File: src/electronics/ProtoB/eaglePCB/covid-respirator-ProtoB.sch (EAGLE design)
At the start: 59 parts, among them IC1 AD825R, IC2 L7805CV-DG, IC3 AD8607R, IC4 AD8607R, T2 BC548

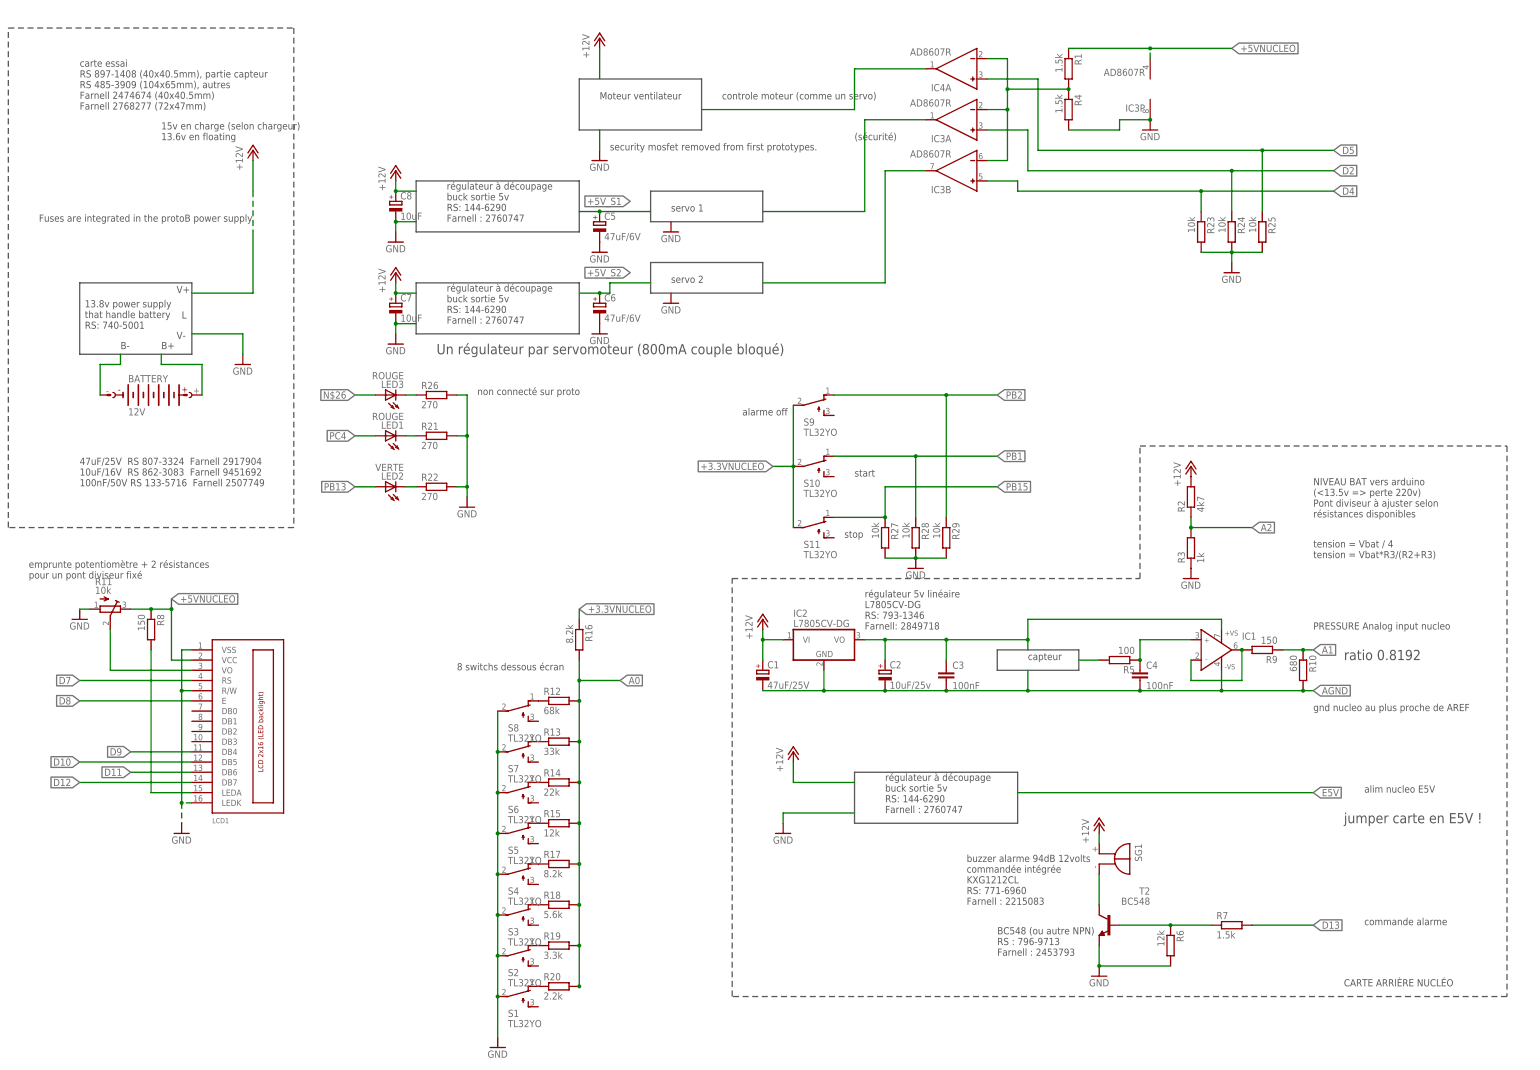
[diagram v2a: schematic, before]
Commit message: update protoB schematic
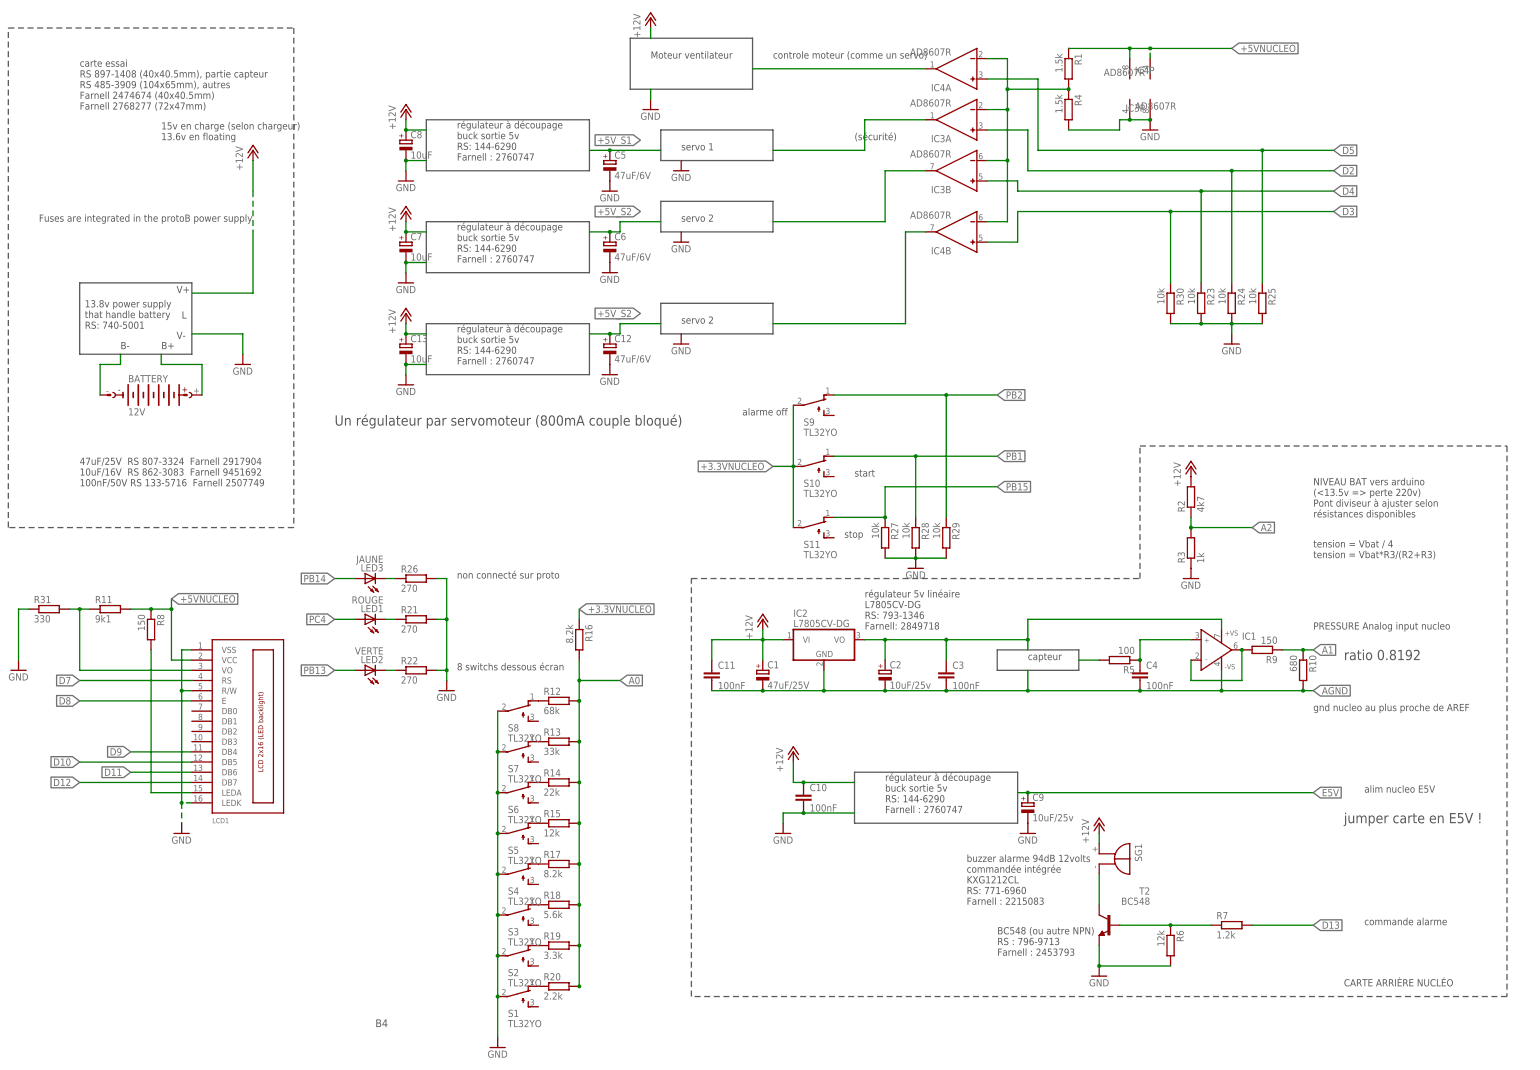
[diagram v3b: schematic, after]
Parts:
- added C10, C11: 100nF, rcl:C-EU050-050X075
- added C12: 47uF/6V, rcl:CPOL-EU150CLZ-1010
- added C13: 10uF, rcl:CPOL-EU150CLZ-1010
- added C9: 10uF/25v, rcl:CPOL-EU150CLZ-1010
- added R30: 10k, rcl:R-EU_0207/10
- added R31: 330, rcl:R-EU_0207/10
- LED3: value ROUGE -> JAUNE
- R11: value 10k -> 9k1; device pot:TRIM_EU-SM-42/43B -> rcl:R-EU_0207/10
- R7: value 1.5k -> 1.2k
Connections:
- net N$26 renamed PB14
- new net D3: IC4B.IN+, R30.1
- new net E5V: C9.+
- new net N$17: IC4B.OUT
- net +12V: now also C10.1, C11.1, C13.+
- net +5VNUCLEO: now also IC4P.V+, R11.2; no longer R11.E
- net +5V_S2: now also C12.+
- net AGND: now also C11.2
- net GND: now also C10.2, C12.-, C13.-, C9.-, IC4P.V-, R30.2, R31.1; no longer R11.A
- net N$10: now also R11.1, R31.2; no longer R11.S
- net N$4: now also IC4B.IN-
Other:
- note added: "B4"
- note removed: "emprunte potentiomètre + 2 résistances pour un pont diviseur fixé"
- note removed: "security mosfet removed from first prototypes."
- moved on the sheet: C5, C6, C7, C8, LED1, LED2, LED3, R21, R22, R23, R24, R25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

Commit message: schematic B5
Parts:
- added R32: 12k, rcl:R-EU_0207/10
- added R33: 100R, rcl:R-EU_0207/10
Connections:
- new net N$25: LCD1.DB7, R33.1
- new net PA13: LCD1.R/W, R32.2
- net D12: now also R33.2; no longer LCD1.DB7
- net GND: now also R32.1; no longer LCD1.R/W
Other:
- note added: "B5"
- note removed: "B4"
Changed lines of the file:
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@@
 <part name="R11" library="rcl" deviceset="R-EU_" device="0207/10" value="9k1"/>
 <part name="R31" library="rcl" deviceset="R-EU_" device="0207/10" value="330"/>
+<part name="R32" library="rcl" deviceset="R-EU_" device="0207/10" value="12k"/>
+<part name="R33" library="rcl" deviceset="R-EU_" device="0207/10" value="100R"/>
 </parts>
 <sheets>
@@
 <text x="152.4" y="15.24" size="1.778" layer="97">start</text>
 <text x="149.86" y="0" size="1.778" layer="97">stop</text>
-<text x="33.02" y="-121.92" size="1.9304" layer="97">B4</text>
+<text x="33.02" y="-121.92" size="1.9304" layer="97">B5</text>
 <wire x1="45.72" y1="53.34" x2="86.36" y2="53.34" width="0.1524" layer="97"/>
 <wire x1="86.36" y1="53.34" x2="86.36" y2="40.64" width="0.1524" layer="97"/>
@@
 <instance part="LCD1" gate="G$1" x="0" y="-27.94"/>
 <instance part="R8" gate="G$1" x="-22.86" y="-22.86" rot="R270"/>
-<instance part="GND11" gate="1" x="-15.24" y="-73.66"/>
+<instance part="GND11" gate="1" x="-15.24" y="-81.28"/>
 <instance part="GND12" gate="1" x="-55.88" y="-33.02"/>
 <instance part="S1" gate="BEF1" x="68.58" y="-114.3" rot="R270"/>
@@
 <instance part="R11" gate="G$1" x="-33.02" y="-17.78"/>
 <instance part="R31" gate="G$1" x="-48.26" y="-17.78"/>
+<instance part="R32" gate="G$1" x="-25.4" y="-71.12" rot="R90"/>
+<instance part="R33" gate="G$1" x="-40.64" y="-60.96" rot="R180"/>
 </instances>
 <busses>
@@
 <pinref part="GND11" gate="1" pin="GND"/>
 <wire x1="-12.7" y1="-66.04" x2="-15.24" y2="-66.04" width="0.1524" layer="91" style="longdash"/>
-<wire x1="-15.24" y1="-66.04" x2="-15.24" y2="-71.12" width="0.1524" layer="91" style="longdash"/>
-<wire x1="-15.24" y1="-66.04" x2="-15.24" y2="-38.1" width="0.1524" layer="91"/>
+<wire x1="-15.24" y1="-66.04" x2="-15.24" y2="-76.2" width="0.1524" layer="91" style="longdash"/>
+<wire x1="-15.24" y1="-76.2" x2="-15.24" y2="-78.74" width="0.1524" layer="91" style="longdash"/>
+<wire x1="-15.24" y1="-66.04" x2="-15.24" y2="-27.94" width="0.1524" layer="91"/>
 <junction x="-15.24" y="-66.04"/>
 <pinref part="LCD1" gate="G$1" pin="VSS"/>
-<wire x1="-15.24" y1="-38.1" x2="-15.24" y2="-27.94" width="0.1524" layer="91"/>
 <wire x1="-15.24" y1="-27.94" x2="-12.7" y2="-27.94" width="0.1524" layer="91"/>
-<pinref part="LCD1" gate="G$1" pin="R/W"/>
-<wire x1="-12.7" y1="-38.1" x2="-15.24" y2="-38.1" width="0.1524" layer="91"/>
-<junction x="-15.24" y="-38.1"/>
+<pinref part="R32" gate="G$1" pin="1"/>
+<wire x1="-25.4" y1="-76.2" x2="-15.24" y2="-76.2" width="0.1524" layer="91"/>
+<junction x="-15.24" y="-76.2"/>
 </segment>
 <segment>
@@
 <net name="D12" class="0">
 <segment>
-<pinref part="LCD1" gate="G$1" pin="DB7"/>
-<wire x1="-12.7" y1="-60.96" x2="-40.64" y2="-60.96" width="0.1524" layer="91"/>
-<label x="-40.64" y="-60.96" size="1.778" layer="95" rot="R180" xref="yes"/>
+<label x="-53.34" y="-60.96" size="1.778" layer="95" rot="R180" xref="yes"/>
+<pinref part="R33" gate="G$1" pin="2"/>
+<wire x1="-45.72" y1="-60.96" x2="-53.34" y2="-60.96" width="0.1524" layer="91"/>
 </segment>
 </net>
@@
 </segment>
 </net>
+<net name="PA13" class="0">
+<segment>
+<pinref part="LCD1" gate="G$1" pin="R/W"/>
+<wire x1="-12.7" y1="-38.1" x2="-25.4" y2="-38.1" width="0.1524" layer="91"/>
+<label x="-33.02" y="-38.1" size="1.778" layer="95" rot="R180" xref="yes"/>
+<pinref part="R32" gate="G$1" pin="2"/>
+<wire x1="-25.4" y1="-38.1" x2="-33.02" y2="-38.1" width="0.1524" layer="91"/>
+<wire x1="-25.4" y1="-66.04" x2="-25.4" y2="-38.1" width="0.1524" layer="91"/>
+<junction x="-25.4" y="-38.1"/>
+</segment>
+</net>
+<net name="N$25" class="0">
+<segment>
+<pinref part="R33" gate="G$1" pin="1"/>
+<pinref part="LCD1" gate="G$1" pin="DB7"/>
+<wire x1="-35.56" y1="-60.96" x2="-12.7" y2="-60.96" width="0.1524" layer="91"/>
+</segment>
+</net>

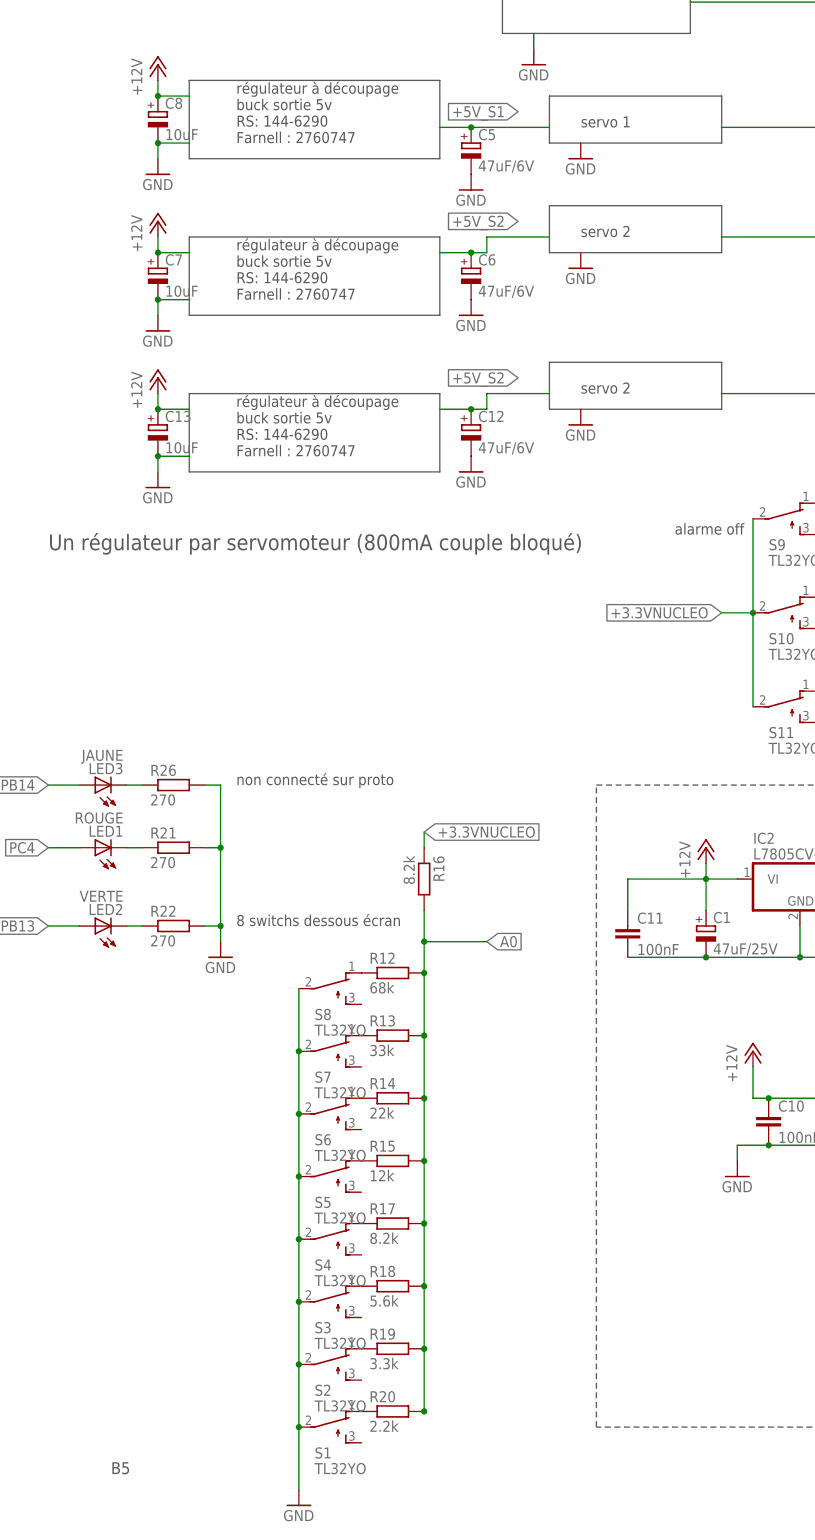
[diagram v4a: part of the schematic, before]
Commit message: schematic B6 with servo names
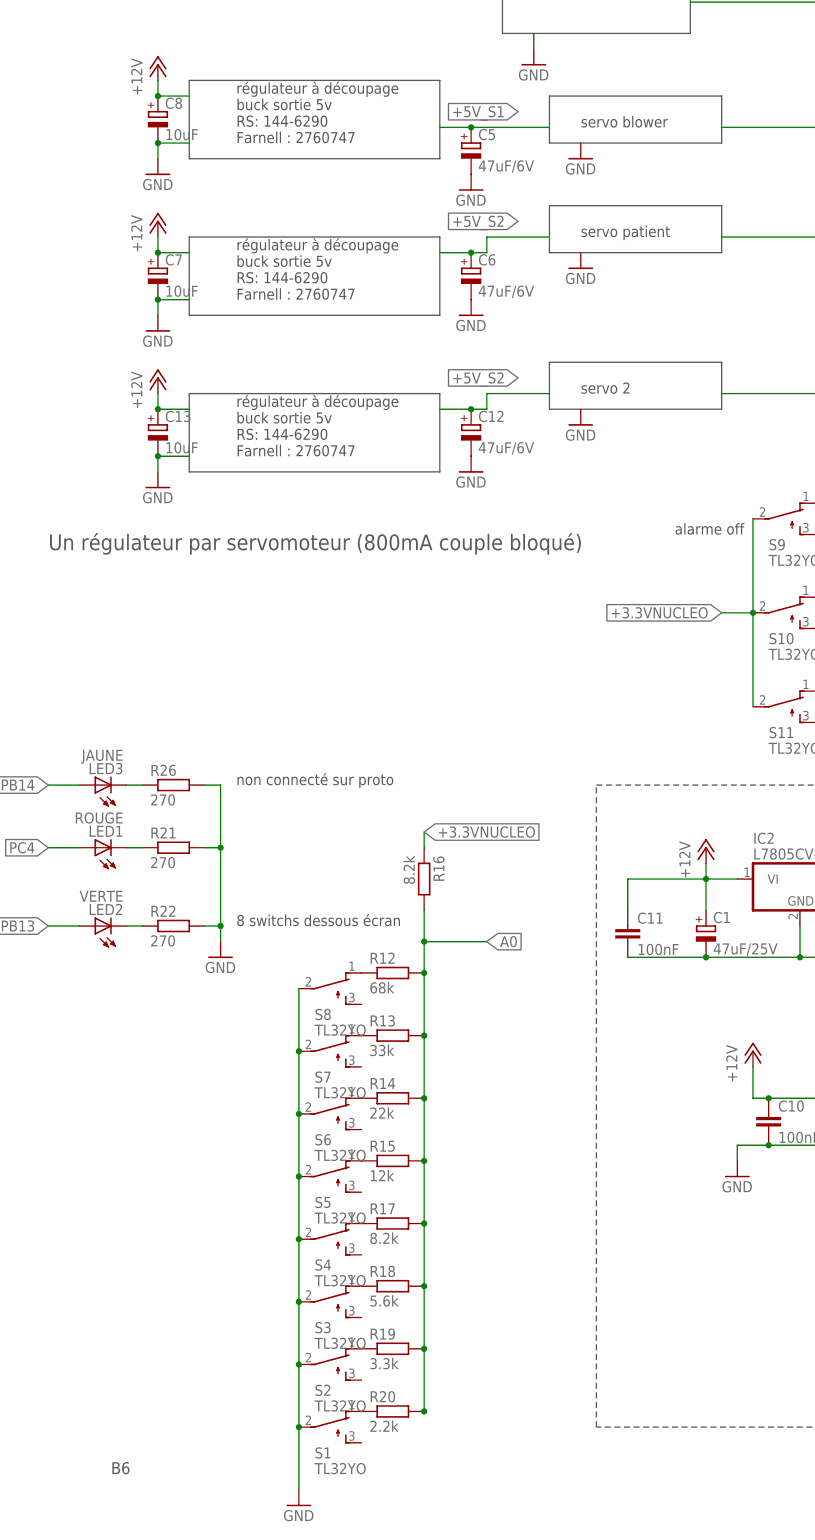
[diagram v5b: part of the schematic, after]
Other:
- note added: "B6"
- note added: "servo blower"
- note added: "servo patient"
- note removed: "B5"
- note removed: "servo 1"
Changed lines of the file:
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@@
 <wire x1="132.08" y1="76.2" x2="104.14" y2="76.2" width="0.1524" layer="97"/>
 <wire x1="104.14" y1="76.2" x2="104.14" y2="83.82" width="0.1524" layer="97"/>
-<text x="109.22" y="96.52" size="1.778" layer="97">servo 1</text>
-<text x="109.22" y="78.74" size="1.778" layer="97">servo 2</text>
+<text x="109.22" y="96.52" size="1.778" layer="97">servo blower</text>
+<text x="109.22" y="78.74" size="1.778" layer="97">servo patient</text>
 <wire x1="-58.42" y1="127" x2="12.7" y2="127" width="0.1524" layer="97" style="longdash"/>
 <wire x1="12.7" y1="127" x2="12.7" y2="2.54" width="0.1524" layer="97" style="longdash"/>
@@
 <text x="152.4" y="15.24" size="1.778" layer="97">start</text>
 <text x="149.86" y="0" size="1.778" layer="97">stop</text>
-<text x="33.02" y="-121.92" size="1.9304" layer="97">B5</text>
+<text x="33.02" y="-121.92" size="1.9304" layer="97">B6</text>
 <wire x1="45.72" y1="53.34" x2="86.36" y2="53.34" width="0.1524" layer="97"/>
 <wire x1="86.36" y1="53.34" x2="86.36" y2="40.64" width="0.1524" layer="97"/>
